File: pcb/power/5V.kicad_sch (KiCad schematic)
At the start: 13 parts, among them U201 TPS62933

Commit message: update ALL parts
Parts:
- C201, C202: LCSC (none) -> C13585
- C203, C205, C208: LCSC (none) -> C28233
- C204: LCSC (none) -> C1739
- C206, C207: LCSC (none) -> C12891
- R201: LCSC C352230 -> (none); MOUSER (none) -> 667-ERA-6AED49R9V
- R202: LCSC C352230 -> (none); MOUSER (none) -> 71-CRCW080553K6FKEA
- R203: LCSC C352230 -> (none); MOUSER (none) -> 667-ERA-6AEB1022V
- U201: LCSC (none) -> C3200405
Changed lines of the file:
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@@
+			)
+		)
+		(property "MOUSER" ""
+			(at 168.91 78.74 0)
+			(effects
+				(font
+					(size 1.27 1.27)
+				)
 			)
 		)
@@
 			)
 		)
-		(property "LCSC" ""
+		(property "LCSC" "C1739"
 			(at 114.3 93.98 0)
 			(effects
@@
 				)
 				(hide yes)
+			)
+		)
+		(property "MOUSER" ""
+			(at 114.3 93.98 0)
+			(effects
+				(font
+					(size 1.27 1.27)
+				)
 			)
 		)
@@
 			)
 		)
-		(property "LCSC" ""
+		(property "LCSC" "C12891"
 			(at 196.85 83.82 0)
 			(effects
@@
 				)
 				(hide yes)
+			)
+		)
+		(property "MOUSER" ""
+			(at 196.85 83.82 0)
+			(effects
+				(font
+					(size 1.27 1.27)
+				)
 			)
 		)
@@
 			)
 		)
-		(property "LCSC" ""
+		(property "LCSC" "C28233"
 			(at 92.71 83.82 0)
 			(effects
@@
 				)
 				(hide yes)
+			)
+		)
+		(property "MOUSER" ""
+			(at 92.71 83.82 0)
+			(effects
+				(font
+					(size 1.27 1.27)
+				)
 			)
 		)
@@
 			)
 		)
+		(property "LCSC" "C3200405"
+			(at 139.7 86.36 0)
+			(effects
+				(font
+					(size 1.27 1.27)
+				)
+			)
+		)
+		(property "MOUSER" ""
+			(at 139.7 86.36 0)
+			(effects
+				(font
+					(size 1.27 1.27)
+				)
+			)
+		)
 		(pin "6"
 		)
@@
 			)
 		)
-		(property "LCSC" "C352230"
+		(property "LCSC" ""
 			(at 173.99 92.71 0)
 			(effects
@@
 				)
 				(hide yes)
+			)
+		)
+		(property "MOUSER" "71-CRCW080553K6FKEA"
+			(at 173.99 92.71 0)
+			(effects
+				(font
+					(size 1.27 1.27)
+				)
 			)
 		)
@@
 			)
 		)
-		(property "LCSC" ""
+		(property "LCSC" "C13585"
 			(at 72.39 83.82 0)
 			(effects
@@
 				)
 				(hide yes)
+			)
+		)
+		(property "MOUSER" ""
+			(at 72.39 83.82 0)
+			(effects
+				(font
+					(size 1.27 1.27)
+				)
 			)
 		)
@@
 			)
 		)
-		(property "LCSC" ""
+		(property "LCSC" "C12891"
 			(at 185.42 83.82 0)
 			(effects
@@
 				)
 				(hide yes)
+			)
+		)
+		(property "MOUSER" ""
+			(at 185.42 83.82 0)
+			(effects
+				(font
+					(size 1.27 1.27)
+				)
 			)
 		)
@@
 			)
 		)
-		(property "LCSC" ""
+		(property "LCSC" "C13585"
 			(at 82.55 83.82 0)
 			(effects
@@
 				)
 				(hide yes)
+			)
+		)
+		(property "MOUSER" ""
+			(at 82.55 83.82 0)
+			(effects
+				(font
+					(size 1.27 1.27)
+				)
 			)
 		)
@@
 			)
 		)
-		(property "LCSC" ""
+		(property "LCSC" "C28233"
 			(at 154.94 78.74 0)
 			(effects
@@
 				)
 				(hide yes)
+			)
+		)
+		(property "MOUSER" ""
+			(at 154.94 78.74 0)
+			(effects
+				(font
+					(size 1.27 1.27)
+				)
 			)
 		)
@@
 			)
 		)
-		(property "LCSC" "C352230"
+		(property "LCSC" ""
 			(at 173.99 102.87 0)
 			(effects
@@
 				)
 				(hide yes)
+			)
+		)
+		(property "MOUSER" "667-ERA-6AEB1022V"
+			(at 173.99 102.87 0)
+			(effects
+				(font
+					(size 1.27 1.27)
+				)
 			)
 		)
@@
 			)
 		)
-		(property "LCSC" "C352230"
+		(property "LCSC" ""
 			(at 173.99 83.82 0)
 			(effects
@@
 				)
 				(hide yes)
+			)
+		)
+		(property "MOUSER" "667-ERA-6AED49R9V"
+			(at 173.99 83.82 0)
+			(effects
+				(font
+					(size 1.27 1.27)
+				)
 			)
 		)
@@
 			)
 		)
-		(property "LCSC" ""
+		(property "LCSC" "C28233"
 			(at 208.28 83.82 0)
 			(effects
@@
 			)
 		)
+		(property "MOUSER" ""
+			(at 208.28 83.82 0)
+			(effects
+				(font
+					(size 1.27 1.27)
+				)
+			)
+		)

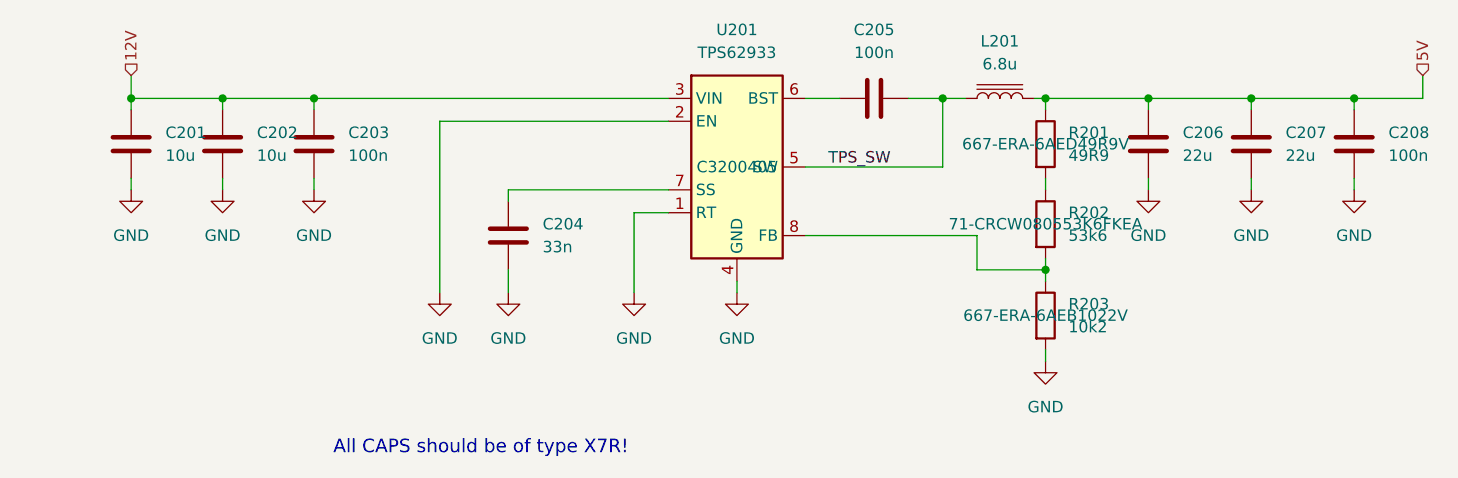
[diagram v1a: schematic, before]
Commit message: fix power, pin 2
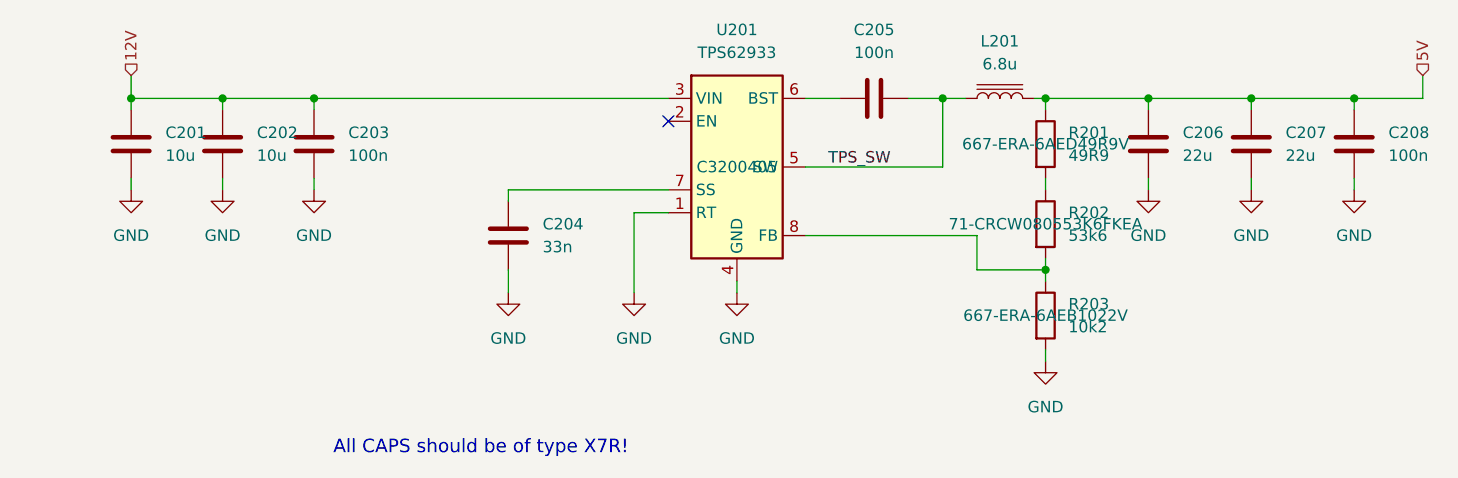
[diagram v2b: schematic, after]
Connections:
- net GND: no longer U201.2 (EN)
- no-connect marks 0 -> 1
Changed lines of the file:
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@@
 		(color 0 0 0 0)
 	)
+	(no_connect
+		(at 132.08 81.28)
+	)
 	(wire
 		(pts
@@
 	(wire
 		(pts
-			(xy 106.68 81.28) (xy 106.68 100.33)
-		)
-		(stroke
-			(width 0)
-			(type default)
-		)
-	)
-	(wire
-		(pts
 			(xy 72.39 78.74) (xy 72.39 80.01)
 		)
@@
 		(pts
 			(xy 132.08 91.44) (xy 128.27 91.44)
-		)
-		(stroke
-			(width 0)
-			(type default)
-		)
-	)
-	(wire
-		(pts
-			(xy 132.08 81.28) (xy 106.68 81.28)
 		)
 		(stroke
@@
 					(unit 1)
 				)
-			)
-		)
-	)
-	(symbol
-		(lib_id "power:GND")
-		(at 106.68 100.33 0)
-		(unit 1)
-		(exclude_from_sim no)
-		(in_bom yes)
-		(on_board yes)
-		(dnp no)
-		(fields_autoplaced yes)
-		(property "Reference" "#PWR0204"
-			(at 106.68 106.68 0)
-			(effects
-				(font
-					(size 1.27 1.27)
-				)
-				(hide yes)
-			)
-		)
-		(property "Value" "GND"
-			(at 106.68 105.41 0)
-			(effects
-				(font
-					(size 1.27 1.27)
-				)
-			)
-		)
-		(property "Footprint" ""
-			(at 106.68 100.33 0)
-			(effects
-				(font
-					(size 1.27 1.27)
-				)
-				(hide yes)
-			)
-		)
-		(property "Datasheet" ""
-			(at 106.68 100.33 0)
-			(effects
-				(font
-					(size 1.27 1.27)
-				)
-				(hide yes)
-			)
-		)
-		(property "Description" "Power symbol creates a global label with name \"GND\" , ground"
-			(at 106.68 100.33 0)
-			(effects
-				(font
-					(size 1.27 1.27)
-				)
-				(hide yes)
-			)
-		)
-		(pin "1"
-		)
-		(instances
-			(project "power"
-				(path "/f29935ff-76ad-48dd-a9d8-f60fd99054e1/a8cb03e0-4cc2-4198-b2d7-2036db94b475"
-					(reference "#PWR0204")
-					(unit 1)
-				)

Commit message: update power pcb
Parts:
- removed C204: 33n, Capacitor_SMD:C_0805_2012Metric, symbol Device:C
- removed U201: TPS62933, Package_TO_SOT_SMD:SOT-583-8, symbol Regulator_Switching:TPS62933
- added C104: 100u / 25V, Capacitor_Tantalum_SMD:CP_EIA-7343-43_Kemet-X, symbol Device:C_Polarized
- added U203: LMR51430 500kHz, Package_TO_SOT_SMD:SOT-23-6, symbol Regulator_Switching:LMR51430
- R202: value 53k6 -> 100k; MOUSER 71-CRCW080553K6FKEA -> (none)
- R203: value 10k2 -> 13k7; MOUSER 667-ERA-6AEB1022V -> (none)
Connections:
- net 12V: now also C104.1, U203.3 (VIN), U203.5 (EN)
- net GND: now also C104.2, U203.1 (GND)
- net TPS_SW: now also U203.2 (SW)
- net at C205.1: now also U203.6 (CB)
- net at R202.2, R203.1: now also U203.4 (FB)
- no-connect marks 1 -> 0
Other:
- moved on the sheet: C201, C202, C203
